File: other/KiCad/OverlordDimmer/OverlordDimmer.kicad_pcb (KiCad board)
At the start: 2 copper layers, 155.1 x 86.1 mm, 185 parts, among them J1 Connector_Screw_Terminal_01x09, J2 USB_cable, J3 RJ45x2, J4 Connector_Screw_Terminal_01x09, J5 USB_B, J6 Conn_01x12_Female, Q1 IRF740, Q10 IRF740, Q11 IRF740, Q12 IRF740, Q13 2N3906, Q14 IRF740, Q15 2N3904, Q16 IRF740, Q17 2N3906, Q18 2N3904, Q19 IRF740, Q2 2N3904, Q20 IRF740, Q21 2N7002E, Q22 2N7002E, Q23 2N3904, Q24 IRF740, Q25 IRF740, Q26 2N3904, Q27 IRF740, Q28 IRF740, Q29 2N3906, Q3 2N3906, Q30 2N3904, Q31 2N3906, Q32 IRF740, Q33 2N3906, Q34 2N3904, Q35 IRF740, Q36 IRF740, Q37 2N3904, Q38 2N3906, Q39 IRF740, Q4 IRF740, Q40 IRF740, Q41 2N3906, Q42 IRF740, Q43 2SC4061KT146N, Q44 BC817, Q45 2SC4061KT146N, Q5 IRF740, Q6 2N3906, Q7 2N3904, Q8 2N3904, Q9 2N3906, U1 4N25, U10 4N25, U11 4N25, U12 4N35, U2 4N25, U3 4N25, U4 SN65HVD230, U5 4N25, U6 4N25, U7 4N25, U8 4N25, U9 4N25

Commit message: Final commit from laptop
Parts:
- added D18: BZX84C12LT1G, Package_TO_SOT_SMD:SOT-23, F.Cu at (186.2, 49.5)
- added J6: Conn_01x12_Pin, Connector_Molex:Molex_Picoflex_90325-0012_2x06_P1.27mm_Vertical, F.Cu at (192.7, 79.1)
- C1, C10, C11, C13, C2, C3, C5, C6, C7, C8: footprint Capacitor_SMD:C_0402_1005Metric_Pad0.74x0.62mm_HandSolder -> Capacitor_SMD:CP_Elec_3x5.4
- R10, R14, R15, R16, R20, R24, R26, R27, R29, R3, R34, R37, R4, R40, R42, R48, R51, R53, R54, R58, R62, R7: footprint Resistor_SMD:R_0402_1005Metric_Pad0.72x0.64mm_HandSolder -> Resistor_SMD:R_0805_2012Metric_Pad1.20x1.40mm_HandSolder
- R17, R18, R28, R31, R39, R41, R43, R5, R52, R55, R64, R65, R66: footprint Resistor_SMD:R_1206_3216Metric_Pad1.30x1.75mm_HandSolder -> Resistor_SMD:R_0805_2012Metric_Pad1.20x1.40mm_HandSolder
- R44, R45, R59, R60, R61, R63: footprint Resistor_SMD:R_1210_3225Metric_Pad1.30x2.65mm_HandSolder -> Resistor_SMD:R_0805_2012Metric_Pad1.20x1.40mm_HandSolder
- moved D14 0.09 mm to (164.4, 44.3), turned to -90 degrees
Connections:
- D14 pad 1: Net-(D14-K) -> L
- D14 pad 2: L -> Net-(D14-A)
- D15 pad 1: N -> Net-(D15-K)
- D15 pad 2: Net-(D15-A) -> N
- J1 pad 1: /triggerCircuit6/Load -> /Load_9
- J1 pad 2: /triggerCircuit5/Load -> /Load
- J1 pad 3: /triggerCircuit4/Load -> /Load_6
- J1 pad 5: /triggerCircuit3/Load -> /Load_5
- J1 pad 7: /triggerCircuit2/Load -> /Load_8
- J1 pad 9: /triggerCircuit1/Load -> /Load_7
- J4 pad 4: /triggerCircuit10/Load -> /Load_4
- J4 pad 6: /triggerCircuit9/Load -> /Load_1
- J4 pad 8: /triggerCircuit8/Load -> /Load_3
- J4 pad 9: /triggerCircuit7/Load -> /Load_2
- Q1 pad 2: L -> Load
- Q10 pad 2: /triggerCircuit2/Load -> /triggerCircuit2/N
- Q11 pad 2: L -> Load
- Q12 pad 2: /triggerCircuit3/Load -> /triggerCircuit3/N
- Q14 pad 2: /triggerCircuit5/Load -> /triggerCircuit5/N
- Q16 pad 2: L -> Load
- Q19 pad 2: L -> Load
- Q20 pad 2: /triggerCircuit4/Load -> /triggerCircuit4/N
- Q24 pad 2: /triggerCircuit6/Load -> /triggerCircuit6/N
- Q25 pad 2: L -> Load
- Q27 pad 2: /triggerCircuit7/Load -> /triggerCircuit7/N
- Q28 pad 2: L -> Load
- Q32 pad 2: L -> Load
- Q35 pad 2: L -> Load
- Q36 pad 2: /triggerCircuit8/Load -> /triggerCircuit8/N
- Q39 pad 2: L -> Load
- Q4 pad 2: /triggerCircuit1/Load -> /triggerCircuit1/N
- Q40 pad 2: /triggerCircuit9/Load -> /triggerCircuit9/N
- Q42 pad 2: /triggerCircuit10/Load -> /triggerCircuit10/N
- Q43 pad 3: Net-(D14-K) -> Net-(D15-K)
- Q45 pad 1: Net-(D15-A) -> Net-(D18-K)
- Q5 pad 2: L -> Load
- R60 pad 1: Net-(D14-K) -> Net-(Q43-B)
- R60 pad 2: Net-(Q43-B) -> Net-(D15-K)
- R61 pad 1: Net-(Q43-B) -> Net-(D18-K)
- R61 pad 2: Net-(D15-A) -> Net-(Q43-B)
- R64 pad 1: Net-(J6-Pin_12) -> Net-(J6-Pin_1)
- R65 pad 1: Net-(J6-Pin_11) -> Net-(J6-Pin_2)
- R66 pad 1: Net-(J6-Pin_10) -> Net-(J6-Pin_3)
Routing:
- net (no net): track 0.00 -> 315.2 mm
- net /triggerCircuit9/Load: track 44.3 -> 0.00 mm
- net /triggerCircuit10/Load: track 42.1 -> 0.00 mm
- net /triggerCircuit8/Load: track 38.5 -> 0.00 mm
- net /triggerCircuit7/Load: track 33.8 -> 0.00 mm
- net /triggerCircuit6/Load: track 33.4 -> 0.00 mm
- net /triggerCircuit5/Load: track 25.6 -> 0.00 mm
- net Net-(D15-A): track 18.6 -> 0.00 mm, vias 2 -> 0
- net /triggerCircuit4/Load: track 18.3 -> 0.00 mm
- net /triggerCircuit3/Load: track 16.9 -> 0.00 mm
- net /triggerCircuit2/Load: track 16.2 -> 0.00 mm
- net /triggerCircuit1/Load: track 15.4 -> 0.00 mm
- net Net-(D14-K): track 11.9 -> 0.00 mm
- net Net-(D15-K): vias 0 -> 2

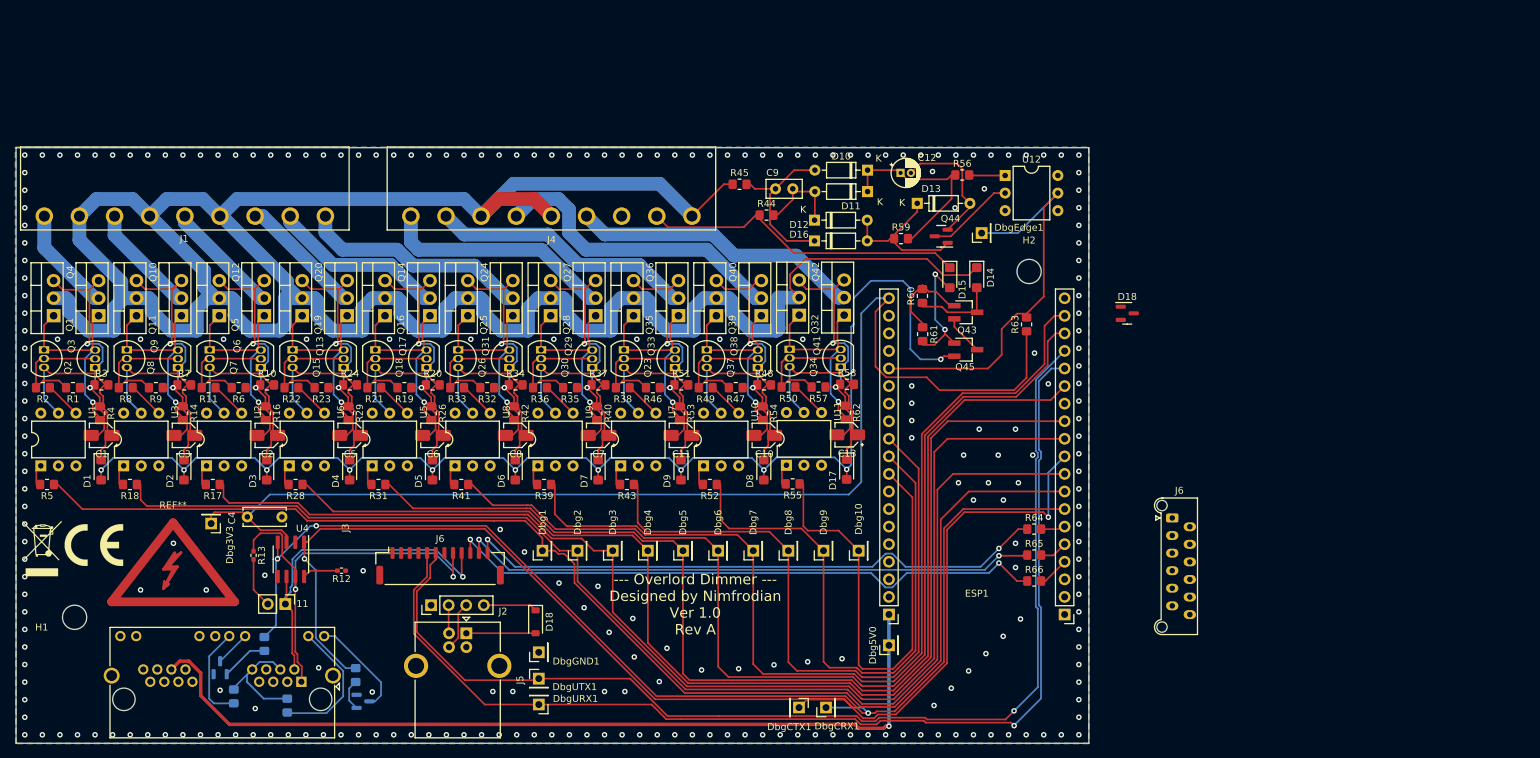
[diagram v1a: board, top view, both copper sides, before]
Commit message: uploadable code, serial communication OK TODO: check pin and functionality compatibility
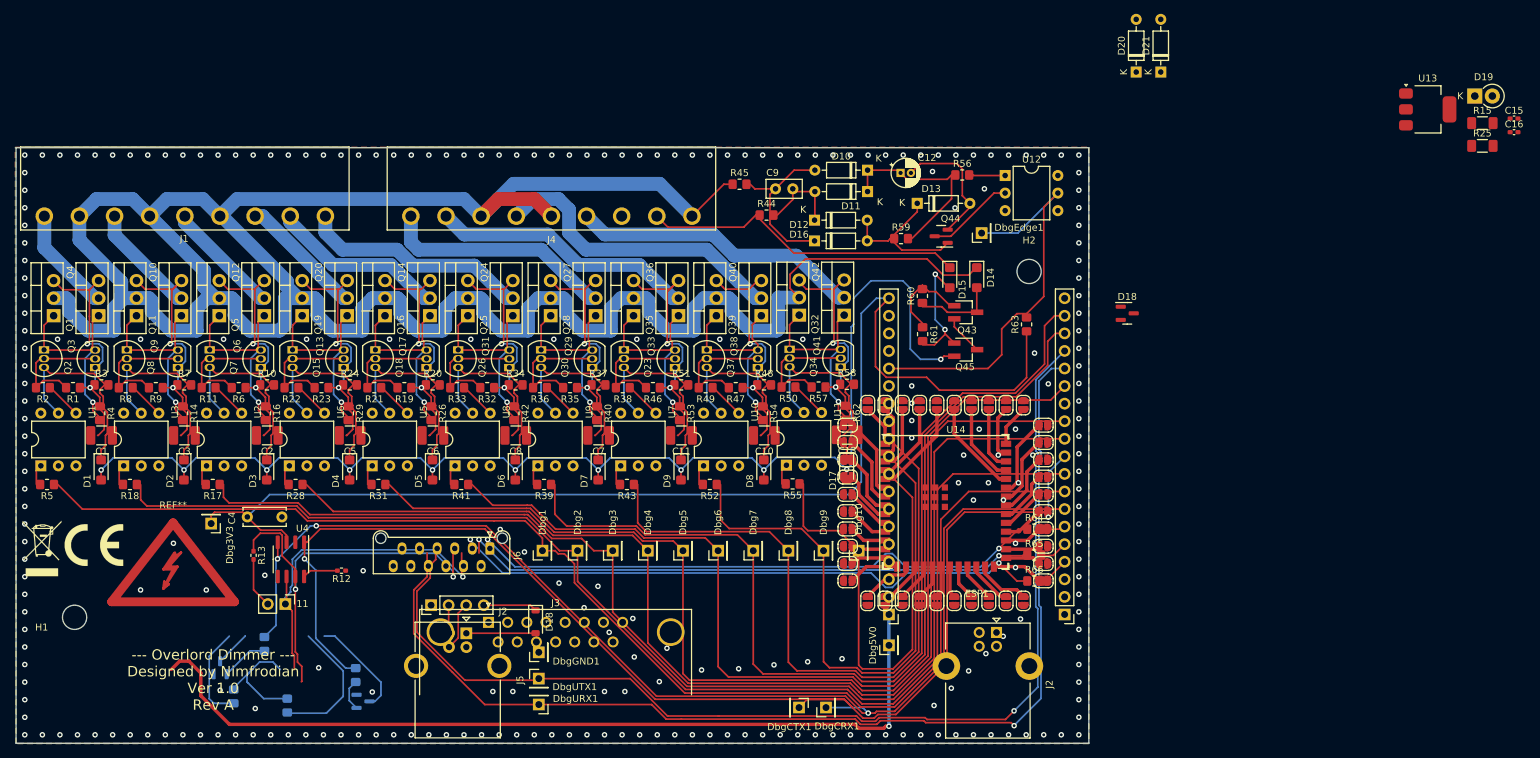
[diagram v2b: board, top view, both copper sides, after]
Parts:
- removed the J6 at (86.8, 86.0)
- added C15: 1uF, Capacitor_SMD:C_0402_1005Metric_Pad0.74x0.62mm_HandSolder, F.Cu at (242.1, 21.3)
- added C16: 1uF, Capacitor_SMD:C_0402_1005Metric_Pad0.74x0.62mm_HandSolder, F.Cu at (242.1, 23.3)
- added D19: 1N4002, Diode_THT:D_DO-41_SOD81_P2.54mm_Vertical_KathodeUp, F.Cu at (236.4, 18.1)
- added D20: 1N4148, Diode_THT:D_DO-35_SOD27_P7.62mm_Horizontal, F.Cu at (187.4, 14.6)
- added D21: 1N4148, Diode_THT:D_DO-35_SOD27_P7.62mm_Horizontal, F.Cu at (191.0, 14.6)
- added J2: USB_B, Connector_USB:USB_B_Lumberg_2411_02_Horizontal, F.Cu at (167.2, 95.6)
- added JP1: SolderJumper_2_Open, Jumper:SolderJumper-2_P1.3mm_Open_RoundedPad1.0x1.5mm, F.Cu at (171.1, 62.8)
- added JP10: SolderJumper_2_Open, Jumper:SolderJumper-2_P1.3mm_Open_RoundedPad1.0x1.5mm, F.Cu at (174.0, 75.7)
- added JP11: SolderJumper_2_Open, Jumper:SolderJumper-2_P1.3mm_Open_RoundedPad1.0x1.5mm, F.Cu at (174.0, 78.2)
- added JP12: SolderJumper_2_Open, Jumper:SolderJumper-2_P1.3mm_Open_RoundedPad1.0x1.5mm, F.Cu at (174.0, 80.7)
- added JP13: SolderJumper_2_Open, Jumper:SolderJumper-2_P1.3mm_Open_RoundedPad1.0x1.5mm, F.Cu at (174.0, 83.2)
- added JP14: SolderJumper_2_Open, Jumper:SolderJumper-2_P1.3mm_Open_RoundedPad1.0x1.5mm, F.Cu at (174.0, 85.7)
- added JP15: SolderJumper_2_Open, Jumper:SolderJumper-2_P1.3mm_Open_RoundedPad1.0x1.5mm, F.Cu at (145.7, 85.7)
- added JP16: SolderJumper_2_Open, Jumper:SolderJumper-2_P1.3mm_Open_RoundedPad1.0x1.5mm, F.Cu at (145.7, 83.2)
- added JP17: SolderJumper_2_Open, Jumper:SolderJumper-2_P1.3mm_Open_RoundedPad1.0x1.5mm, F.Cu at (145.7, 80.7)
- added JP18: SolderJumper_2_Open, Jumper:SolderJumper-2_P1.3mm_Open_RoundedPad1.0x1.5mm, F.Cu at (145.7, 78.2)
- added JP19: SolderJumper_2_Open, Jumper:SolderJumper-2_P1.3mm_Open_RoundedPad1.0x1.5mm, F.Cu at (145.7, 75.7)
- added JP2: SolderJumper_2_Open, Jumper:SolderJumper-2_P1.3mm_Open_RoundedPad1.0x1.5mm, F.Cu at (168.6, 62.8)
- added JP20: SolderJumper_2_Open, Jumper:SolderJumper-2_P1.3mm_Open_RoundedPad1.0x1.5mm, F.Cu at (145.7, 73.2)
- added JP21: SolderJumper_2_Open, Jumper:SolderJumper-2_P1.3mm_Open_RoundedPad1.0x1.5mm, F.Cu at (145.7, 70.7)
- added JP22: SolderJumper_2_Open, Jumper:SolderJumper-2_P1.3mm_Open_RoundedPad1.0x1.5mm, F.Cu at (145.7, 68.2)
- added JP23: SolderJumper_2_Open, Jumper:SolderJumper-2_P1.3mm_Open_RoundedPad1.0x1.5mm, F.Cu at (145.7, 65.7)
- added JP24: SolderJumper_2_Open, Jumper:SolderJumper-2_P1.3mm_Open_RoundedPad1.0x1.5mm, F.Cu at (158.6, 62.8)
- added JP25: SolderJumper_2_Open, Jumper:SolderJumper-2_P1.3mm_Open_RoundedPad1.0x1.5mm, F.Cu at (156.1, 62.8)
- added JP26: SolderJumper_2_Open, Jumper:SolderJumper-2_P1.3mm_Open_RoundedPad1.0x1.5mm, F.Cu at (153.6, 62.8)
- added JP27: SolderJumper_2_Open, Jumper:SolderJumper-2_P1.3mm_Open_RoundedPad1.0x1.5mm, F.Cu at (151.1, 62.8)
- added JP28: SolderJumper_2_Open, Jumper:SolderJumper-2_P1.3mm_Open_RoundedPad1.0x1.5mm, F.Cu at (148.6, 62.8)
- added JP29: SolderJumper_2_Open, Jumper:SolderJumper-2_P1.3mm_Open_RoundedPad1.0x1.5mm, F.Cu at (174.0, 88.2)
- added JP3: SolderJumper_2_Open, Jumper:SolderJumper-2_P1.3mm_Open_RoundedPad1.0x1.5mm, F.Cu at (166.1, 62.8)
- added JP30: SolderJumper_2_Open, Jumper:SolderJumper-2_P1.3mm_Open_RoundedPad1.0x1.5mm, F.Cu at (171.1, 91.1)
- added JP31: SolderJumper_2_Open, Jumper:SolderJumper-2_P1.3mm_Open_RoundedPad1.0x1.5mm, F.Cu at (168.6, 91.1)
- added JP32: SolderJumper_2_Open, Jumper:SolderJumper-2_P1.3mm_Open_RoundedPad1.0x1.5mm, F.Cu at (166.1, 91.1)
- added JP33: SolderJumper_2_Open, Jumper:SolderJumper-2_P1.3mm_Open_RoundedPad1.0x1.5mm, F.Cu at (163.6, 91.1)
- added JP34: SolderJumper_2_Open, Jumper:SolderJumper-2_P1.3mm_Open_RoundedPad1.0x1.5mm, F.Cu at (161.1, 91.1)
- added JP35: SolderJumper_2_Open, Jumper:SolderJumper-2_P1.3mm_Open_RoundedPad1.0x1.5mm, F.Cu at (158.6, 91.1)
- added JP36: SolderJumper_2_Open, Jumper:SolderJumper-2_P1.3mm_Open_RoundedPad1.0x1.5mm, F.Cu at (156.1, 91.1)
- added JP37: SolderJumper_2_Open, Jumper:SolderJumper-2_P1.3mm_Open_RoundedPad1.0x1.5mm, F.Cu at (153.6, 91.1)
- added JP38: SolderJumper_2_Open, Jumper:SolderJumper-2_P1.3mm_Open_RoundedPad1.0x1.5mm, F.Cu at (151.1, 91.1)
- added JP39: SolderJumper_2_Open, Jumper:SolderJumper-2_P1.3mm_Open_RoundedPad1.0x1.5mm, F.Cu at (148.6, 91.1)
- added JP4: SolderJumper_2_Open, Jumper:SolderJumper-2_P1.3mm_Open_RoundedPad1.0x1.5mm, F.Cu at (163.6, 62.8)
- added JP40: SolderJumper_2_Open, Jumper:SolderJumper-2_P1.3mm_Open_RoundedPad1.0x1.5mm, F.Cu at (145.7, 88.2)
- added JP5: SolderJumper_2_Open, Jumper:SolderJumper-2_P1.3mm_Open_RoundedPad1.0x1.5mm, F.Cu at (161.1, 62.8)
- added JP6: SolderJumper_2_Open, Jumper:SolderJumper-2_P1.3mm_Open_RoundedPad1.0x1.5mm, F.Cu at (174.0, 65.7)
- added JP7: SolderJumper_2_Open, Jumper:SolderJumper-2_P1.3mm_Open_RoundedPad1.0x1.5mm, F.Cu at (174.0, 68.2)
- added JP8: SolderJumper_2_Open, Jumper:SolderJumper-2_P1.3mm_Open_RoundedPad1.0x1.5mm, F.Cu at (174.0, 70.7)
- added JP9: SolderJumper_2_Open, Jumper:SolderJumper-2_P1.3mm_Open_RoundedPad1.0x1.5mm, F.Cu at (174.0, 73.2)
- added R15: 240, Resistor_SMD:R_1206_3216Metric_Pad1.30x1.75mm_HandSolder, F.Cu at (237.5, 22.0)
- added R25: 390, Resistor_SMD:R_1206_3216Metric_Pad1.30x1.75mm_HandSolder, F.Cu at (237.5, 25.3)
- added U13: LM317_SOT-223, Package_TO_SOT_SMD:SOT-223-3_TabPin2, F.Cu at (229.6, 20.0)
- added U14: ESP32S3-Wroom, PCM_Espressif:ESP32-S3-WROOM-1U, F.Cu at (159.9, 76.6)
- C1, C10, C11, C13, C2, C3, C5, C6, C7, C8: footprint Capacitor_SMD:CP_Elec_3x5.4 -> Capacitor_SMD:C_1210_3225Metric_Pad1.33x2.70mm_HandSolder
- J3: value RJ45x2 -> DE15_Plug_HighDensity_MountingHoles; footprint Connector_RJ:RJ45_Amphenol_RJHSE538X-02 -> Connector_Dsub:DSUB-15_Male_Horizontal_P2.77x2.84mm_EdgePinOffset7.70mm_Housed_MountingHolesOffset9.12mm
- moved J6 98.8 mm to (94.0, 83.5), turned to -90 degrees
- moved J3 28.4 mm to (93.8, 94.2), turned to 0 degrees
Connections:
- ESP1 pad 20: +5V -> unconnected-(ESP1-+5V-Pad20)
- J1 pad 1: /Load_9 -> /Load
- J1 pad 2: /Load -> /Load_8
- J1 pad 4: L -> unconnected-(J1-Pin_4-Pad4)
- J1 pad 5: /Load_5 -> /Load_7
- J1 pad 6: L -> unconnected-(J1-Pin_6-Pad6)
- J1 pad 7: /Load_8 -> /Load_5
- J1 pad 8: L -> unconnected-(J1-Pin_8-Pad8)
- J1 pad 9: /Load_7 -> /Load_9
- J3 pad 1: CAN_H -> GND
- J3 pad 10: Net-(J3-Pad10) -> unconnected-(J3-Pad10)
- J3 pad 11: Net-(Q22-D) -> CAN_H
- J3 pad 12: Net-(J3-Pad12) -> MB1_H
- J3 pad 13: unconnected-(J3-Pad13) -> MB2_H
- J3 pad 14: unconnected-(J3-Pad14) -> +12V
- J3 pad 15: unconnected-(J3-Pad15) -> +12V
- J3 pad 2: CAN_L -> MB1_L
- J3 pad 4: +12V -> unconnected-(J3-Pad4)
- J3 pad 5: GND -> unconnected-(J3-Pad5)
- J3 pad 6: unconnected-(J3-Pad6) -> GND
- J3 pad 7: GND -> CAN_L
- J3 pad 8: +12V -> MB2_L
- J3 pad 9: Net-(Q21-D) -> unconnected-(J3-Pad9)
- J4 pad 4: /Load_4 -> /Load_3
- J4 pad 5: L -> unconnected-(J4-Pin_5-Pad5)
- J4 pad 6: /Load_1 -> /Load_4
- J4 pad 7: L -> unconnected-(J4-Pin_7-Pad7)
- J4 pad 8: /Load_3 -> /Load_2
- J4 pad 9: /Load_2 -> /Load_1
- J6 pad 4: CAN_L -> unconnected-(J6-Pin_4-Pad4)
- J6 pad 5: CAN_H -> unconnected-(J6-Pin_5-Pad5)
- J6 pad 7: UART_TX_0 -> unconnected-(J6-Pin_7-Pad7)
- J6 pad 8: UART_RX_0 -> unconnected-(J6-Pin_8-Pad8)
- Q1 pad 2: Load -> L
- Q10 pad 2: /triggerCircuit2/N -> Load
- Q11 pad 2: Load -> L
- Q12 pad 2: /triggerCircuit3/N -> Load
- Q14 pad 2: /triggerCircuit5/N -> Load
- Q16 pad 2: Load -> L
- Q19 pad 2: Load -> L
- Q20 pad 2: /triggerCircuit4/N -> Load
- Q24 pad 2: /triggerCircuit6/N -> Load
- Q25 pad 2: Load -> L
- Q27 pad 2: /triggerCircuit7/N -> Load
- Q28 pad 2: Load -> L
- Q32 pad 2: Load -> L
- Q35 pad 2: Load -> L
- Q36 pad 2: /triggerCircuit8/N -> Load
- Q39 pad 2: Load -> L
- Q4 pad 2: /triggerCircuit1/N -> Load
- Q40 pad 2: /triggerCircuit9/N -> Load
- Q42 pad 2: /triggerCircuit10/N -> Load
- Q5 pad 2: Load -> L
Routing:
- net Net-(J6-Pin_3): track 0.00 -> 88.0 mm, vias 0 -> 2
- net Net-(J6-Pin_10): track 88.0 -> 0.00 mm, vias 2 -> 0
- net Net-(J6-Pin_12): track 85.4 -> 0.00 mm, vias 2 -> 0
- net Net-(J6-Pin_1): track 0.00 -> 85.4 mm, vias 0 -> 2
- net Net-(J6-Pin_2): track 0.00 -> 84.4 mm, vias 0 -> 2
- net Net-(J6-Pin_11): track 84.4 -> 0.00 mm, vias 2 -> 0
- net Net-(JP24-A): track 0.00 -> 13.9 mm
- net Net-(JP5-A): track 0.00 -> 13.7 mm
- net Net-(JP4-A): track 0.00 -> 11.6 mm
- net Net-(JP6-A): track 0.00 -> 11.5 mm
- net Net-(JP23-A): track 0.00 -> 11.5 mm
- net Net-(JP25-A): track 0.00 -> 11.4 mm
- net Net-(JP22-A): track 0.00 -> 10.3 mm
- net Net-(JP7-A): track 0.00 -> 10.2 mm
- net Net-(JP21-A): track 0.00 -> 9.28 mm
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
